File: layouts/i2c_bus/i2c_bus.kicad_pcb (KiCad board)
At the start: 2 copper layers, 2 parts

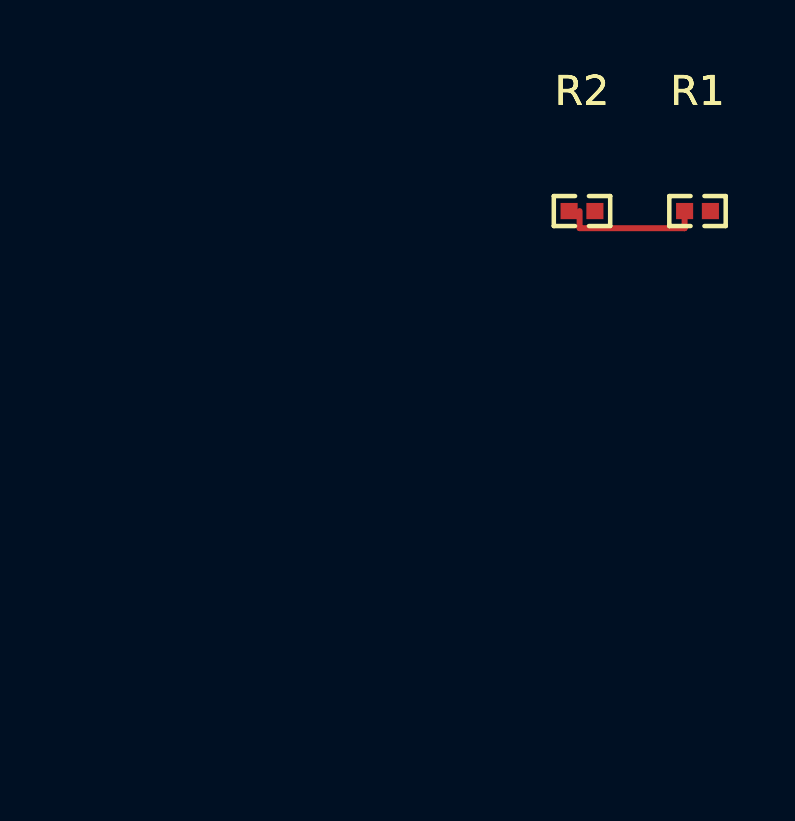
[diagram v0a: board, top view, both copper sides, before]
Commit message: Enhance smart placer with simulated annealing and pre-routing validation
Smart Placer improvements:
- Add simulated annealing refinement (now default) for better wire length optimization
- Add force-directed refinement with improvement safeguard
- Add silkscreen text repositioning to avoid component overlaps
- Significant wire length reductions (e.g., power_filter: 113mm -> 46mm)

Autorouter improvements:
- Add PreRoutingValidator class for pre-flight checks
- Validate unconnected pads, overlapping footprints, unplaced components
- Use pad-based bounds for accurate overlap detection
- Block routing on validation errors with actionable messages

Research:
- Add comprehensive autorouting/autoplacement findings document
- Cover Freerouting Python client, OrthoRoute, DeepPCB, KiCad 9 IPC API
- Document force-directed and simulated annealing algorithms

Cleanup:
- Update .gitignore for DSN/SES files, build artifacts, tools
- Remove stale timestamped build files
- Add parts footprints and symbols

All 10 modules placed and routed successfully.

Co-Authored-By: Claude Opus 4.5 <noreply@anthropic.com>
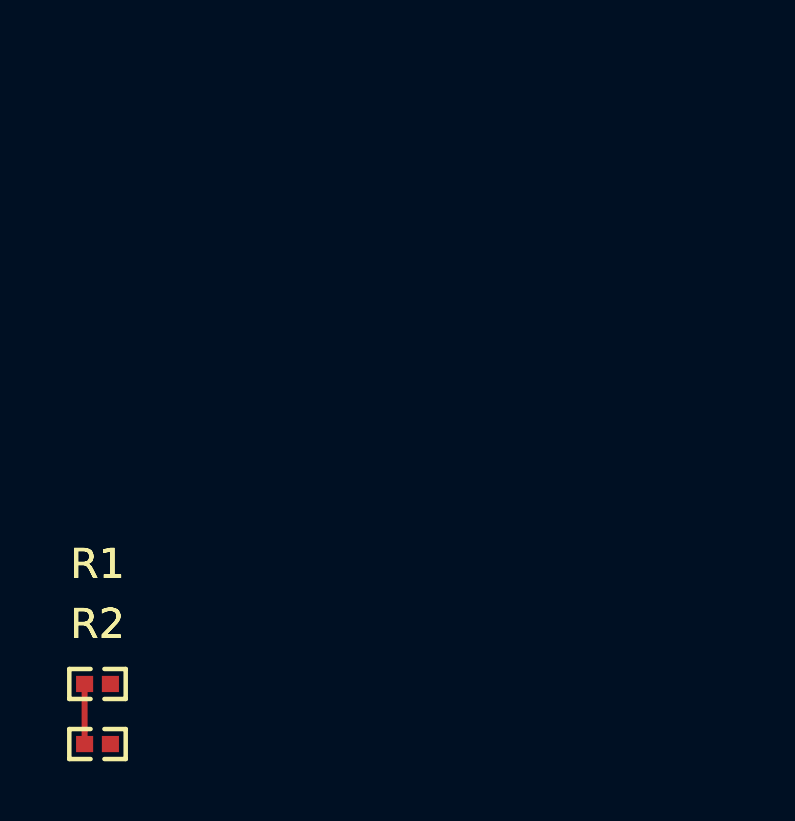
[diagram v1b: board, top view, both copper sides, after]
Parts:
- moved R1 25.5 mm to (80.0, 115.8)
- moved R2 24.0 mm to (80.0, 117.8)
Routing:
- net vcc: track 4.64 -> 2.00 mm
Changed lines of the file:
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@@
 	(footprint "UNI_ROYAL_0402WGF4701TCE:R0402"
 		(layer "F.Cu")
-		(at 100 100)
+		(at 80 115.7643)
 		(property "Reference" "R1"
 			(at 0 -4 0)
@@
 	(footprint "UNI_ROYAL_0402WGF4701TCE:R0402"
 		(layer "F.Cu")
-		(at 96.15 100)
+		(at 80 117.7663)
 		(property "Reference" "R2"
 			(at 0 -4 0)
@@
 	)
 	(segment
-		(start 99.57 100)
-		(end 99.57 100.5717)
+		(start 79.57 117.7663)
+		(end 79.57 115.7643)
 		(width 0.2)
 		(layer "F.Cu")
-		(net 1)
-	)
-	(segment
-		(start 96.07 100)
-		(end 96.07 100.5717)
-		(width 0.2)
-		(layer "F.Cu")
-		(net 1)
-	)
-	(segment
-		(start 96.07 100.5717)
-		(end 99.57 100.5717)
-		(width 0.2)
-		(layer "F.Cu")
